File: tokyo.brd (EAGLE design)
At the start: 115 x 34 mm, 52 parts, among them J1 254-2X5F, J2 254-2X5M, P1 9774050151, P2 9774050151, P3 9774050151, P4 9774050151, Q1 STD6N95K5, T1 750313823, U1 UCC28710, X1 508-1X3B

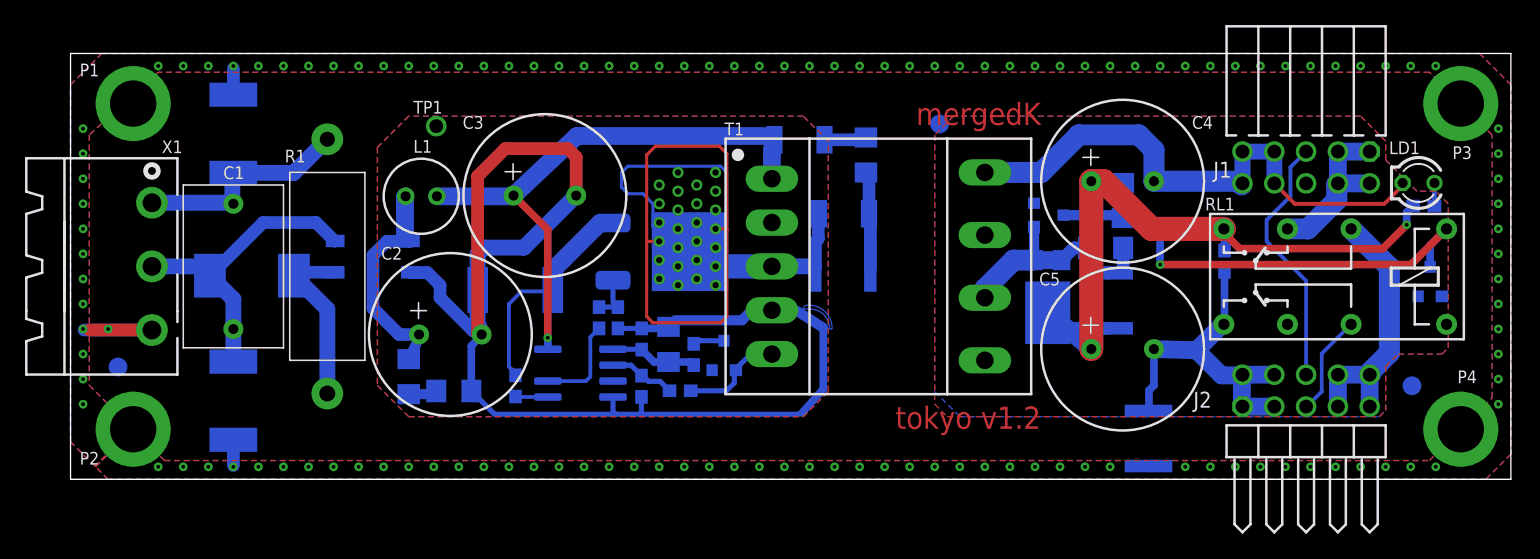
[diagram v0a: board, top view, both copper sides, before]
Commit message: Removed relais, added choke, added dissipation area for output diode, added minimum load circuiRemoved relais, added choke, added dissipation area for output diode, added minimum load circuit.
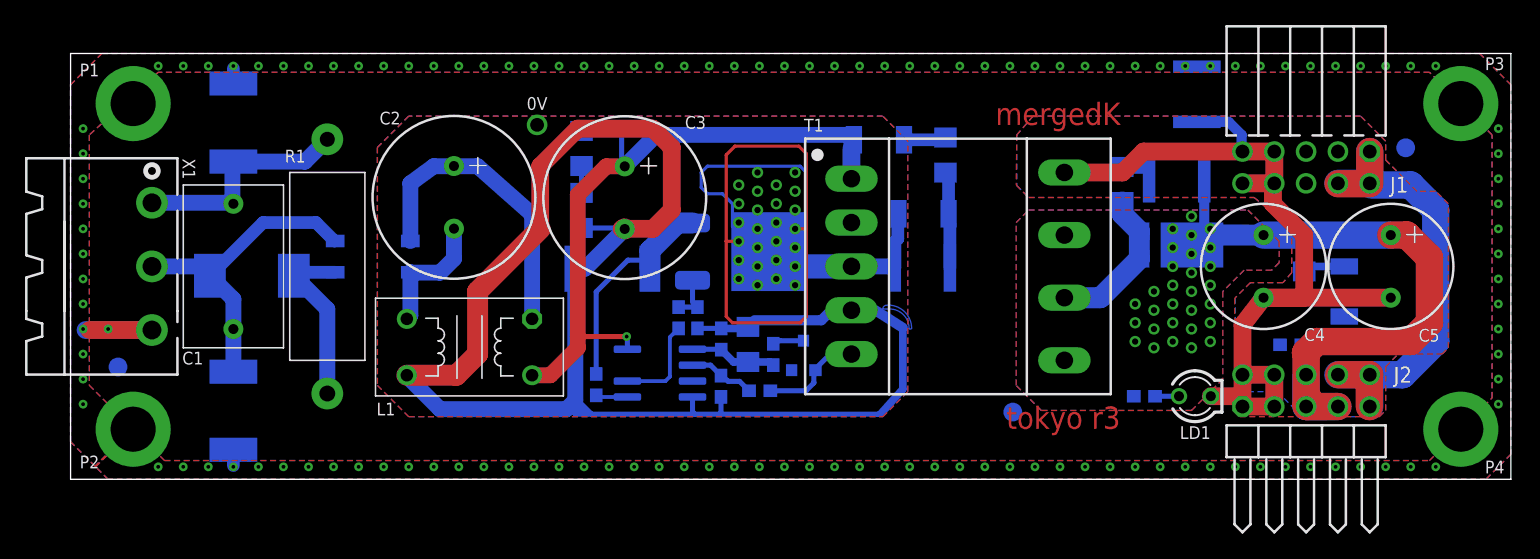
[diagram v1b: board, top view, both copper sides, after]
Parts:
- removed C14: 2200p/250V, capacitors:2211
- removed D8: SMCJ400CA, supressors:DO-214AB
- removed RL1: V23105, relais:V23105
- removed TP1: TESTPOINT, unsorted:TESTPOINT
- added 0V: TESTPOINT, unsorted:TESTPOINT
- added R14: 332k, resistors:1206
- C10: value 1n/2kV -> 10u/50v; device capacitors:1812 -> capacitors:1206
- C11: value 10u/50v -> 100n; device capacitors:1206 -> capacitors:0603
- C12: value 100n -> 2200p/250V; device capacitors:0603 -> capacitors:2211
- C4, C5: value 1800u -> 1500u; device capacitors:D13 -> capacitors:D10
- C8: value 22u -> 1n/2kv; device capacitors:1206 -> capacitors:1812
- C9: value 1n/2kv -> 1n/2kV
- D1: value BAS21 -> 1SMB5919BT3G; device diodes:SOT23 -> diodes:DO-214AA
- D2: value BAS21 -> PDS1040L; device diodes:SOT23 -> diodes:POWERDI5
- D3: value PDS1040L -> SMBJ85A; device diodes:POWERDI5 -> supressors:DO-214AA
- D4: value SMBJ85A -> MURS360S; device supressors:DO-214AA -> diodes:DO-214AA
- D5: value MURS360S -> BAS21; device diodes:DO-214AA -> diodes:SOT23
- D6: value BAS21 -> HD06; device diodes:SOT23 -> diodes:MINIDIP
- D7: value HD06 -> SMCJ400CA; device diodes:MINIDIP -> supressors:DO-214AB
- L1: value 7447462471 -> 744821150; device powermagnetics:7447462471 -> powermagnetics:744821150
- R10: value 1k -> 10
- R12: value 332k -> 1k; device resistors:1206 -> resistors:0603
- R2: value 1k -> 1; device resistors:0603 -> resistors:1206
- R3: value 39 -> 1k; device resistors:1206 -> resistors:0603
- R4: value 130 -> 39
- R5: value 39 -> 130; device resistors:0603 -> resistors:1206
- R6: value 121k -> 39
- R7: value 24k9 -> 121k
- R8: value 10k -> 24k9
- R9: value 10 -> 10k
- moved C12 33.1 mm to (13.0, 5.47), turned to 270 degrees
- moved D6 29.1 mm to (24.1, 17.8), turned to 90 degrees
- moved C7 27.7 mm to (89.9, 30.7), turned to 90 degrees
- moved R5 25.6 mm to (69.9, 25.9), turned to 270 degrees
- moved LD1 24.7 mm to (89.8, 6.64), turned to 0 degrees
- moved FIDUCIAL2 23.7 mm to (75.2, 5.37)
- moved C5 22.4 mm to (105.4, 17.0), turned to 0 degrees
- moved C13 22.2 mm to (13.0, 28.5)
- moved R4 20.6 mm to (84.0, 23.5), turned to 90 degrees
- moved R13 19.1 mm to (40.8, 21.5)
- moved FIDUCIAL1 19.0 mm to (106.6, 26.5)
- moved D5 17.2 mm to (58.5, 9.89), turned to 0 degrees
- moved C9 15.1 mm to (68.0, 16.9), turned to 0 degrees
- moved R10 14.1 mm to (48.5, 12.9)
- moved C4 13.1 mm to (95.2, 17.0), turned to 0 degrees
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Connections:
- removed net N$19: J2.10, J2.7, J2.8, J2.9, RL1.4
- removed net N$22: J1.5, J2.6
- removed net N$27: C8.1, D1.3, D2.3, RL1.1
- new net N$20: C2.2, D6.2, L1.4
- net +5V/1: now also C8.2, D2.P$3, J2.5, J2.6, J2.7, R3.1; no longer C9.2, D3.P$3, RL1.8
- net +5V/2: now also J2.10, J2.8, J2.9; no longer J1.3, RL1.6
- net 0V: now also 0V.P$1, C10.2, L1.3, R13.2, R8.2, R9.1; no longer C12.2, C2.2, D7.2, R12.2, R7.2, R8.1, TP1.P$1
- net 0V/1: now also D1.2; no longer C8.2, D1.1, RL1.16, RL1.9
- net EARTH: now also C12.2, C13.1; no longer C13.2, C14.1
- net N$1: now also C13.2; no longer C14.2
- net N$10: now also D4.2, R5.1; no longer D5.2, R4.1
- net N$11: now also C9.2, D3.1; no longer C10.2, D4.1
- net N$12: now also R12.2; no longer R10.2
- net N$13: now also R12.1; no longer R10.1
- net N$14: now also R10.2; no longer R8.2
- net N$15: now also C10.1, R6.1; no longer C12.1, R5.1
- net N$16: now also D1.1, R2.2; no longer R12.1, R13.2
- net N$17: now also C9.1, D3.2, R5.2; no longer C10.1, D4.2, R4.2
- net N$18: now also R7.2, R8.1; no longer R6.2, R7.1
- net N$2: now also C12.1, D6.4, D7.P$1; no longer C13.1, D7.4, D8.P$1
- net N$21: now also C2.1, D6.1, L1.1; no longer J2.5, RL1.13
- net N$23: now also R10.1; no longer R9.1
- net N$26: now also D5.3, R6.2; no longer D6.3, R5.2
- net N$3: now also D5.1, R7.1; no longer D6.1, R6.1
- net N$4: now also D6.3, D7.P$2; no longer D7.3, D8.P$2
- net N$5: now also R3.2; no longer R2.2
- net N$6: now also C8.1, R4.2; no longer C9.1, R3.2
- net N$7: now also R14.2; no longer C2.1, D7.1, L1.1
- net N$8: now also D2.P$1, D2.P$2, R4.1; no longer D2.1, D3.P$1, D3.P$2, R3.1
- net N$9: now also D4.1, R14.1; no longer D5.1
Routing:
- net N$27: track 38.4 -> 0.00 mm, vias 1 -> 0
- net +5V/2: track 13.9 -> 43.3 mm
- net 0V: track 109.8 -> 136.4 mm
- net N$19: track 23.7 -> 0.00 mm
- net N$22: track 20.4 -> 0.00 mm
- net N$7: track 18.7 -> 2.14 mm
- net N$21: track 8.09 -> 24.6 mm
- net N$20: track 0.00 -> 10.2 mm
- net N$9: track 45.5 -> 55.5 mm
- net +5V/1: track 55.2 -> 61.3 mm, vias 1 -> 29
- net EARTH: track 15.7 -> 14.7 mm, vias 127 -> 129
- net N$16: track 2.26 -> 3.28 mm
- net 0V/1: track 72.1 -> 71.2 mm
- net N$2: track 24.9 -> 25.7 mm
- net N$6: track 3.57 -> 2.98 mm
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- added copper zone on layer 1, net +5V/1
- added copper zone on layer 16, net +5V/1
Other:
- board text added: "tokyo r3"
- board text removed: "tokyo v1.2"

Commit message: Libraries updated.
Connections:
- net +5V/1: now also D2.3; no longer D2.P$3
- net N$8: now also D2.1, D2.2; no longer D2.P$1, D2.P$2
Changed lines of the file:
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@@
 <setting verticaltext="up"/>
 </settings>
-<grid distance="0.5" unitdist="mm" unit="mm" style="lines" multiple="1" display="yes" altdistance="0.1" altunitdist="mm" altunit="mm"/>
+<grid distance="0.05" unitdist="inch" unit="mm" style="lines" multiple="1" display="no" altdistance="0.025" altunitdist="inch" altunit="mm"/>
 <layers>
 <layer number="1" name="Top" color="4" fill="1" visible="yes" active="yes"/>
@@
 <signal name="N$8">
 <contactref element="R4" pad="1"/>
-<contactref element="D2" pad="P$1"/>
-<contactref element="D2" pad="P$2"/>
+<contactref element="D2" pad="1"/>
+<contactref element="D2" pad="2"/>
 <contactref element="T1" pad="7"/>
 <wire x1="79.35" y1="14.5" x2="82.229" y2="14.5" width="1.6764" layer="16"/>
@@
 <contactref element="C6" pad="1"/>
 <contactref element="C8" pad="2"/>
-<contactref element="D2" pad="P$3"/>
+<contactref element="D2" pad="3"/>
 <wire x1="89.537" y1="18.708" x2="90.152" y2="19.508" width="1.6764" layer="16"/>
 <wire x1="90.152" y1="19.508" x2="95.25" y2="19.5" width="1.6764" layer="16"/>

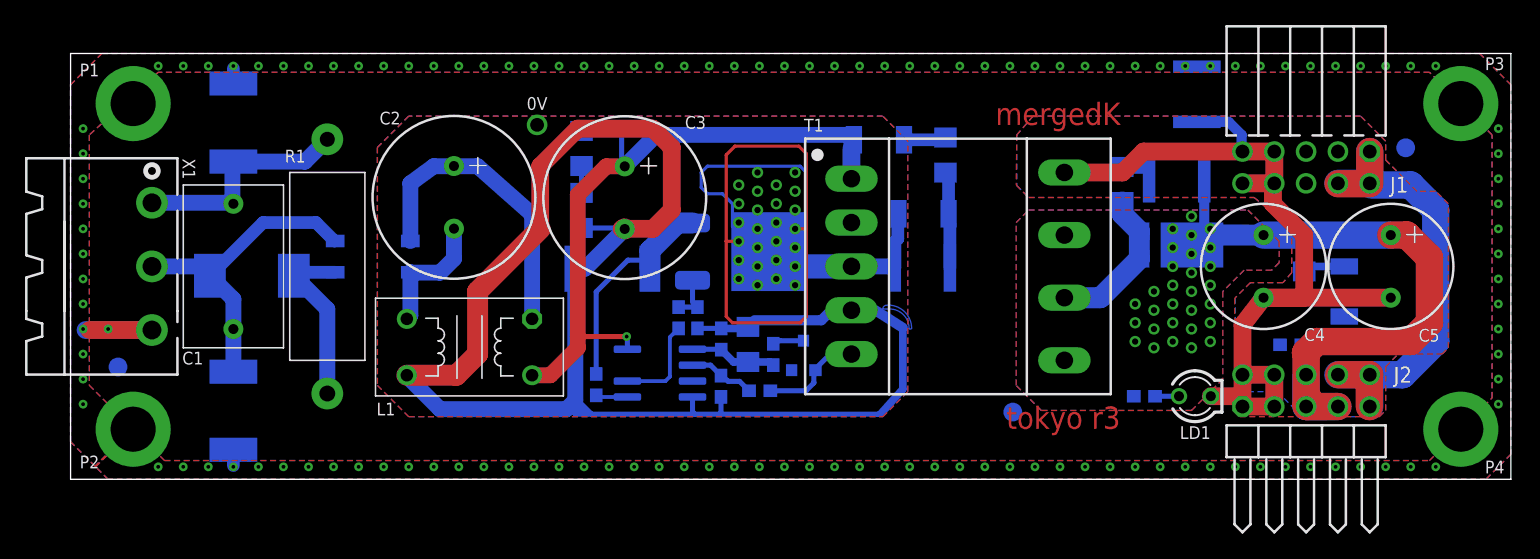
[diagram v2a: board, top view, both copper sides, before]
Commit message: New placement of mounting holes.
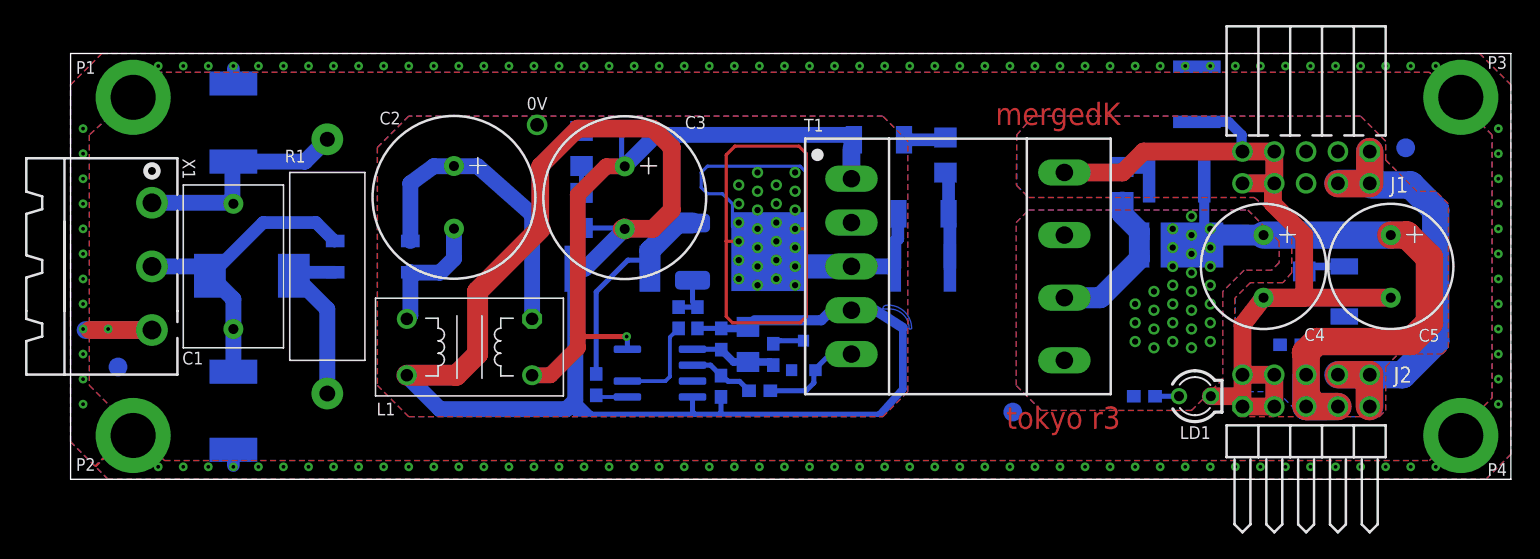
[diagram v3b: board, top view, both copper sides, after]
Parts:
- moved P1 0.50 mm to (5.00, 30.5)
- moved P2 0.50 mm to (5.00, 3.50)
- moved P3 0.50 mm to (111.0, 30.5)
- moved P4 0.50 mm to (111.0, 3.50)
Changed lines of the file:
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@@
 <setting verticaltext="up"/>
 </settings>
-<grid distance="0.05" unitdist="inch" unit="mm" style="lines" multiple="1" display="no" altdistance="0.025" altunitdist="inch" altunit="mm"/>
+<grid distance="0.5" unitdist="mm" unit="mm" style="lines" multiple="1" display="no" altdistance="0.1" altunitdist="mm" altunit="mm"/>
 <layers>
 <layer number="1" name="Top" color="4" fill="1" visible="yes" active="yes"/>
@@
 <attribute name="NAME" x="88.566" y="3.223" size="1.016" layer="25" ratio="10"/>
 </element>
-<element name="P1" library="unsorted" package="9774050151" value="9774050151" x="5" y="30" locked="yes" smashed="yes">
-<attribute name="MF#" value="977 405 015 1" x="5" y="30" size="1.778" layer="27" display="off"/>
-<attribute name="MF" value="Würth Elektronik" x="5" y="30" size="1.778" layer="27" display="off"/>
-<attribute name="NAME" x="0.73" y="32.175" size="1.016" layer="25"/>
-</element>
-<element name="P2" library="unsorted" package="9774050151" value="9774050151" x="5" y="4" locked="yes" smashed="yes">
-<attribute name="MF#" value="977 405 015 1" x="5" y="4" size="1.778" layer="27" display="off"/>
-<attribute name="MF" value="Würth Elektronik" x="5" y="4" size="1.778" layer="27" display="off"/>
-<attribute name="NAME" x="0.73" y="0.875" size="1.016" layer="25"/>
-</element>
-<element name="P3" library="unsorted" package="9774050151" value="9774050151" x="111" y="30" locked="yes" smashed="yes">
-<attribute name="MF#" value="977 405 015 1" x="111" y="30" size="1.778" layer="27" display="off"/>
-<attribute name="MF" value="Würth Elektronik" x="111" y="30" size="1.778" layer="27" display="off"/>
-<attribute name="NAME" x="112.93" y="32.675" size="1.016" layer="25"/>
-</element>
-<element name="P4" library="unsorted" package="9774050151" value="9774050151" x="111" y="4" locked="yes" smashed="yes">
-<attribute name="MF#" value="977 405 015 1" x="111" y="4" size="1.778" layer="27" display="off"/>
-<attribute name="MF" value="Würth Elektronik" x="111" y="4" size="1.778" layer="27" display="off"/>
-<attribute name="NAME" x="112.93" y="0.475" size="1.016" layer="25"/>
+<element name="P1" library="unsorted" package="9774050151" value="9774050151" x="5" y="30.5" locked="yes" smashed="yes">
+<attribute name="MF#" value="977 405 015 1" x="5" y="30.5" size="1.778" layer="27" display="off"/>
+<attribute name="MF" value="Würth Elektronik" x="5" y="30.5" size="1.778" layer="27" display="off"/>
+<attribute name="NAME" x="0.43" y="32.375" size="1.016" layer="25"/>
+</element>
+<element name="P2" library="unsorted" package="9774050151" value="9774050151" x="5" y="3.5" locked="yes" smashed="yes">
+<attribute name="MF#" value="977 405 015 1" x="5" y="3.5" size="1.778" layer="27" display="off"/>
+<attribute name="MF" value="Würth Elektronik" x="5" y="3.5" size="1.778" layer="27" display="off"/>
+<attribute name="NAME" x="0.43" y="0.675" size="1.016" layer="25"/>
+</element>
+<element name="P3" library="unsorted" package="9774050151" value="9774050151" x="111" y="30.5" locked="yes" smashed="yes">
+<attribute name="MF#" value="977 405 015 1" x="111" y="30.5" size="1.778" layer="27" display="off"/>
+<attribute name="MF" value="Würth Elektronik" x="111" y="30.5" size="1.778" layer="27" display="off"/>
+<attribute name="NAME" x="113.13" y="32.775" size="1.016" layer="25"/>
+</element>
+<element name="P4" library="unsorted" package="9774050151" value="9774050151" x="111" y="3.5" locked="yes" smashed="yes">
+<attribute name="MF#" value="977 405 015 1" x="111" y="3.5" size="1.778" layer="27" display="off"/>
+<attribute name="MF" value="Würth Elektronik" x="111" y="3.5" size="1.778" layer="27" display="off"/>
+<attribute name="NAME" x="113.13" y="0.275" size="1.016" layer="25"/>
 </element>
 <element name="Q1" library="transistors" package="DPAK" value="STD6N95K5" x="53.61" y="18.18" smashed="yes" rot="MR180">

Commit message: Revision for manufacturing.
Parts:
- C1: value 220n/275V -> 220n/275Vac; device capacitors:13X8 -> capacitors:14X8
- C12, C13: value 2200p/250V -> 2200p/250Vac
- C7, C9: value 1n/2kV -> 1000p/250Vac
- C8: value 1n/2kv -> 1000p/250Vac
- R11: value 0.5 -> 0.5/0.8W
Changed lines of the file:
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@@
 <setting verticaltext="up"/>
 </settings>
-<grid distance="0.5" unitdist="mm" unit="mm" style="lines" multiple="1" display="no" altdistance="0.1" altunitdist="mm" altunit="mm"/>
+<grid distance="1" unitdist="mm" unit="mm" style="lines" multiple="1" display="no" altdistance="0.1" altunitdist="mm" altunit="mm"/>
 <layers>
 <layer number="1" name="Top" color="4" fill="1" visible="yes" active="yes"/>
@@
 </autorouter>
 <elements>
-<element name="C1" library="capacitors" package="13X8" value="220n/275V" x="13" y="17" smashed="yes" rot="R270">
+<element name="C1" library="capacitors" package="14X8" value="220n/275Vac" x="13" y="17" smashed="yes" rot="R270">
 <attribute name="NAME" x="8.92" y="9.17" size="1.016" layer="25" ratio="10"/>
 </element>
-<element name="C7" library="capacitors" package="1812" value="1n/2kV" x="89.93" y="30.74" smashed="yes" rot="MR90">
+<element name="C7" library="capacitors" package="1812" value="1000p/250Vac" x="89.93" y="30.74" smashed="yes" rot="MR90">
 <attribute name="NAME" x="87.56" y="31.5544" size="1.016" layer="26" ratio="10" rot="MR270"/>
 </element>
-<element name="C9" library="capacitors" package="1812" value="1n/2kV" x="68.01" y="16.88" smashed="yes" rot="MR0">
+<element name="C9" library="capacitors" package="1812" value="1000p/250Vac" x="68.01" y="16.88" smashed="yes" rot="MR0">
 <attribute name="NAME" x="66.9956" y="14.61" size="1.016" layer="26" ratio="10" rot="MR180"/>
 </element>
@@
 <attribute name="NAME" x="96.9756" y="12.795" size="1.016" layer="26" ratio="10" rot="MR180"/>
 </element>
-<element name="C12" library="capacitors" package="2211" value="2200p/250V" x="13" y="5.475" smashed="yes" rot="MR270">
+<element name="C12" library="capacitors" package="2211" value="2200p/250Vac" x="13" y="5.475" smashed="yes" rot="MR270">
 <attribute name="NAME" x="9.65" y="4.435" size="1.016" layer="26" ratio="10" rot="SMR90"/>
 </element>
-<element name="C13" library="capacitors" package="2211" value="2200p/250V" x="13" y="28.485" smashed="yes" rot="MR270">
+<element name="C13" library="capacitors" package="2211" value="2200p/250Vac" x="13" y="28.485" smashed="yes" rot="MR270">
 <attribute name="NAME" x="9.65" y="27.325" size="1.016" layer="26" ratio="10" rot="SMR90"/>
 </element>
@@
 <attribute name="NAME" x="50.728" y="29.001" size="1.016" layer="25" ratio="10" rot="R180"/>
 </element>
-<element name="C8" library="capacitors" package="1812" value="1n/2kv" x="88.315" y="24.005" smashed="yes" rot="MR180">
+<element name="C8" library="capacitors" package="1812" value="1000p/250Vac" x="88.315" y="24.005" smashed="yes" rot="MR180">
 <attribute name="NAME" x="89.5194" y="26.465" size="1.016" layer="26" ratio="10" rot="SMR0"/>
 </element>
@@
 <attribute name="NAME" x="42.475" y="5.7144" size="1.016" layer="26" ratio="10" rot="MR270"/>
 </element>
-<element name="R11" library="resistors" package="2512" value="0.5" x="43.255" y="16.815" smashed="yes" rot="MR180">
+<element name="R11" library="resistors" package="2512" value="0.5/0.8W" x="43.255" y="16.815" smashed="yes" rot="MR180">
 <attribute name="NAME" x="42.465" y="14.665" size="1.016" layer="26" ratio="10" rot="MR180"/>
 </element>
@@
 <element name="L1" library="powermagnetics" package="744821150" value="744821150" x="31.85" y="10.56" smashed="yes">
 <attribute name="NAME" x="24.43" y="5.105" size="1.016" layer="25" ratio="10"/>
+<attribute name="MF#" value="744 821 150" x="31.85" y="10.56" size="1.778" layer="27" display="off"/>
+<attribute name="MF" value="Würth Elektronik" x="31.85" y="10.56" size="1.778" layer="27" display="off"/>
 </element>
 <element name="D1" library="diodes" package="DO-214AA" value="1SMB5919BT3G" x="101.7" y="15" smashed="yes" rot="MR270">
 <attribute name="NAME" x="99.446" y="14.838" size="1.016" layer="26" ratio="10" rot="SMR270"/>
+<attribute name="MOUSER#" value="863-1SMB5919BT3G" x="101.7" y="15" size="1.778" layer="28" rot="MR270" display="off"/>
+<attribute name="MF#" value="1SMB5919BT3G" x="101.7" y="15" size="1.778" layer="28" rot="MR270" display="off"/>
+<attribute name="MF" value="ON Semiconductor" x="101.7" y="15" size="1.778" layer="28" rot="MR270" display="off"/>
 </element>
 <element name="R2" library="resistors" package="1206" value="1" x="98.5" y="18" smashed="yes" rot="MR270">

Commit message: Corrected value for C10.
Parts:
- C10: value 10u/50v -> 10u/50V
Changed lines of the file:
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@@
 <attribute name="NAME" x="66.9956" y="14.61" size="1.016" layer="26" ratio="10" rot="MR180"/>
 </element>
-<element name="C10" library="capacitors" package="1206" value="10u/50v" x="54.085" y="10.77" smashed="yes" rot="MR90">
+<element name="C10" library="capacitors" package="1206" value="10u/50V" x="54.085" y="10.77" smashed="yes" rot="MR90">
 <attribute name="NAME" x="56.4044" y="13.375" size="1.016" layer="26" ratio="10" rot="MR0"/>
 </element>
